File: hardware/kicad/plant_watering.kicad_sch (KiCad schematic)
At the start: 45 parts, among them J1 USB-C POWER IN (5V charger), J10 Pump2_12V, J11 Pump3_12V, J12 Pump4_12V, J13 Pump5_12V, J14 Pump6_12V, J15 Float switch (water level), J2 UI MODULE, J3 Sensor1 (GND,VCC,DIS,OUT), J4 Sensor2 (GND,VCC,DIS,OUT), J5 Sensor3 (GND,VCC,DIS,OUT), J6 Sensor4 (GND,VCC,DIS,OUT), J7 Sensor5 (GND,VCC,DIS,OUT), J8 Sensor6 (GND,VCC,DIS,OUT), J9 Pump1_12V, Q1 IRLZ44N, Q2 IRLZ44N, Q3 IRLZ44N, Q4 IRLZ44N, Q5 IRLZ44N, Q6 IRLZ44N, U1 YD-ESP32-23

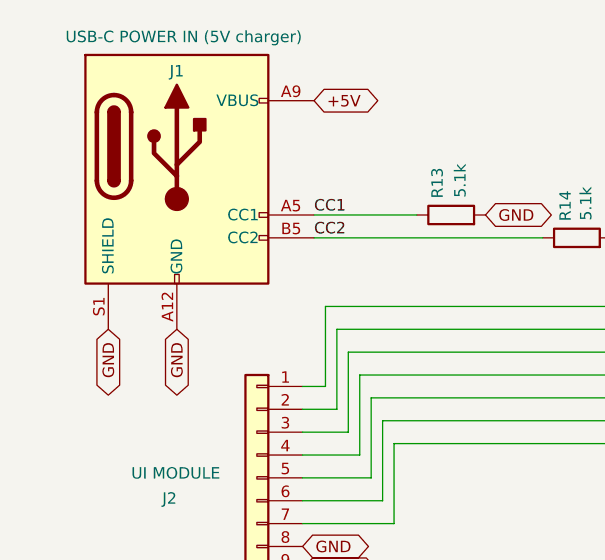
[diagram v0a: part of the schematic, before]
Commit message: Mount UI module on the PCB, panel USB-C input, extra mounting holes
- J2: replace the JST-XH 9-pin with a 1x9 2.54 mm socket plus the UI
  module's four M3 standoff holes (new UI_module_OLED_EC11 footprint);
  the module plugs in face-up left of the ESP32 and screws down
- Board widened to 143 x 112 mm for the module; UI nets rerouted,
  corner holes moved, three extra M3 holes beside J3-J8 against flex
- J1: JST-PH 6-pin for a panel-mount USB-C socket cable
- MT3608 footprint updated to measured hole spacing (26 x 13 mm)
- README/BOM: UI module photo and mounting notes, ESP pinout and
  IN-OUT jumper warning, 1:1 printable board PDF

Co-Authored-By: Claude Opus 5.5 <noreply@anthropic.com>
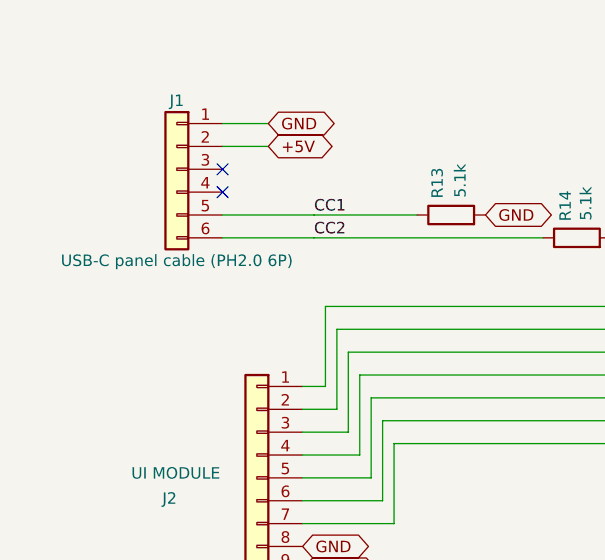
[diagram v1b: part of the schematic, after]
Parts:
- removed J1: USB-C POWER IN (5V charger), Connector_USB:USB_C_Receptacle_GCT_USB4125-xx-x-0190_6P_TopMnt_Horizontal, symbol Connector:USB_C_Receptacle_PowerOnly_6P
- added J1: USB-C panel cable (PH2.0 6P), Connector_JST:JST_PH_B6B-PH-K_1x06_P2.00mm_Vertical, symbol Connector_Generic:Conn_01x06
- J2: footprint Connector_JST:JST_XH_B9B-XH-A_1x09_P2.50mm_Vertical -> plant_watering_parts:UI_module_OLED_EC11
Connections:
- net +5V: now also J1.2 (Pin_2)
- net CC1: now also J1.5 (Pin_5)
- net CC2: now also J1.6 (Pin_6)
- net GND: now also J1.1 (Pin_1)
- no-connect marks 0 -> 2
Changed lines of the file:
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@@
 	(wire
 		(pts
+			(xy 34.29 26.67) (xy 39.37 26.67)
+		)
+		(stroke
+			(width 0)
+			(type default)
+		)
+	)
+	(wire
+		(pts
+			(xy 34.29 29.21) (xy 39.37 29.21)
+		)
+		(stroke
+			(width 0)
+			(type default)
+		)
+	)
+	(wire
+		(pts
+			(xy 34.29 36.83) (xy 44.45 36.83)
+		)
+		(stroke
+			(width 0)
+			(type default)
+		)
+	)
+	(wire
+		(pts
+			(xy 34.29 39.37) (xy 44.45 39.37)
+		)
+		(stroke
+			(width 0)
+			(type default)
+		)
+	)
+	(no_connect
+		(at 34.29 31.75)
+	)
+	(no_connect
+		(at 34.29 34.29)
+	)
+	(wire
+		(pts
 			(xy 118.11 80.01) (xy 124.46 80.01)
 		)
@@
 	(global_label "GND"
 		(shape bidirectional)
-		(at 29.21 49.53 270)
+		(at 39.37 26.67 0)
 		(effects
 			(font
 				(size 1.27 1.27)
 			)
-			(justify right)
+			(justify left)
 		)
 		(property "Intersheetrefs" "${INTERSHEET_REFS}"
-			(at 29.21 49.53 0)
+			(at 39.37 26.67 0)
 			(hide yes)
 			(show_name no)
@@
 	(global_label "+5V"
 		(shape bidirectional)
-		(at 44.45 24.13 0)
+		(at 39.37 29.21 0)
 		(effects
 			(font
@@
 		)
 		(property "Intersheetrefs" "${INTERSHEET_REFS}"
-			(at 44.45 24.13 0)
+			(at 39.37 29.21 0)
 			(hide yes)
 			(show_name no)
@@
 		)
 	)
-	(global_label "GND"
-		(shape bidirectional)
-		(at 21.59 49.53 270)
-		(effects
-			(font
-				(size 1.27 1.27)
-			)
-			(justify right)
-		)
-		(property "Intersheetrefs" "${INTERSHEET_REFS}"
-			(at 21.59 49.53 0)
-			(hide yes)
-			(show_name no)
-			(do_not_autoplace no)
-			(effects
-				(font
-					(size 1.27 1.27)
-				)
-			)
-		)
-	)
 	(global_label "+3V3"
 		(shape bidirectional)
@@
 	)
 	(symbol
-		(lib_id "Connector:USB_C_Receptacle_PowerOnly_6P")
-		(at 29.21 31.75 0)
-		(unit 1)
-		(body_style 1)
-		(exclude_from_sim no)
-		(in_bom yes)
-		(on_board yes)
-		(in_pos_files yes)
-		(dnp no)
-		(property "Reference" "J1"
-			(at 29.21 21.59 0)
-			(show_name no)
-			(do_not_autoplace no)
-			(effects
-				(font
-					(size 1.27 1.27)
-				)
-				(justify bottom)
-			)
-		)
-		(property "Value" "USB-C POWER IN (5V charger)"
-			(at 29.972 17.78 0)
-			(show_name no)
-			(do_not_autoplace no)
-			(effects
-				(font
-					(size 1.27 1.27)
-				)
-				(justify bottom)
-			)
-		)
-		(property "Footprint" "Connector_USB:USB_C_Receptacle_GCT_USB4125-xx-x-0190_6P_TopMnt_Horizontal"
-			(at 33.02 34.29 0)
-			(hide yes)
-			(show_name no)
-			(do_not_autoplace no)
-			(effects
-				(font
-					(size 1.27 1.27)
-				)
-			)
-		)
-		(property "Datasheet" "https://www.usb.org/sites/default/files/documents/usb_type-c.zip"
-			(at 29.21 31.75 0)
-			(hide yes)
-			(show_name no)
-			(do_not_autoplace no)
-			(effects
-				(font
-					(size 1.27 1.27)
-				)
-			)
-		)
-		(property "Description" "USB Power-Only 6P Type-C Receptacle connector"
-			(at 29.21 31.75 0)
-			(hide yes)
-			(show_name no)
-			(do_not_autoplace no)
-			(effects
-				(font
-					(size 1.27 1.27)
-				)
-			)
-		)
-		(pin "A12"
-		)
-		(pin "A5"
-		)
-		(pin "A9"
-		)
-		(pin "B12"
-		)
-		(pin "B5"
-		)
-		(pin "B9"
-		)
-		(pin "S1"
-		)
-		(instances
-			(project "plant_watering"
-				(path "/44c71f65-c0c8-415d-9be8-1e5a85110f51"
-					(reference "J1")
-					(unit 1)
-				)
-			)
-		)
-	)
-	(symbol
 		(lib_id "Diode:1N5819")
 		(at 254 163.83 90)
@@
 			)
 		)
-		(property "Footprint" "Connector_JST:JST_XH_B9B-XH-A_1x09_P2.50mm_Vertical"
+		(property "Footprint" "plant_watering_parts:UI_module_OLED_EC11"
 			(at 38.1 66.04 0)
 			(hide yes)
@@
           (unit 1)
         )
+      )
+    )
+  )
+    (symbol (lib_id "Connector_Generic:Conn_01x06") (at 29.21 31.75 0) (mirror y) (unit 1)
+    (body_style 1) (exclude_from_sim no) (in_bom yes) (on_board yes) (in_pos_files yes) (dnp no)
+    (property "Reference" "J1"
+      (at 29.21 24.13 0)
+      (show_name no)
+      (do_not_autoplace no)
+      (effects
+    				(font
+    					(size 1.27 1.27)
+    				)
+    			)
+    )
+    (property "Value" "USB-C panel cable (PH2.0 6P)"
+      (at 29.21 41.91 0)
+      (show_name no)
+      (do_not_autoplace no)
+      (effects
+    				(font
+    					(size 1.27 1.27)
+    				)
+    			)
+    )
+    (property "Footprint" "Connector_JST:JST_PH_B6B-PH-K_1x06_P2.00mm_Vertical"
+      (at 29.21 31.75 0)
+      (hide yes)
+      (show_name no)
+      (do_not_autoplace no)
+      (effects
+    				(font
+    					(size 1.27 1.27)
+    				)
+    			)
+    )
+    (property "Datasheet" "https://www.usb.org/sites/default/files/documents/usb_type-c.zip"
+      (at 29.21 31.75 0)
+      (hide yes)
+      (show_name no)
+      (do_not_autoplace no)
+      (effects
+    				(font
+    					(size 1.27 1.27)
+    				)
+    			)
+    )
+    (property "Description" "USB Power-Only 6P Type-C Receptacle connector"
+      (at 29.21 31.75 0)
+      (hide yes)
+      (show_name no)
+      (do_not_autoplace no)
+      (effects
+    				(font
+    					(size 1.27 1.27)
+    				)
+    			)
+    )
+    (pin "1")
+    (pin "2")
+    (pin "3")
+    (pin "4")
+    (pin "5")
+    (pin "6")
+    (instances
+      (project "plant_watering"
+        (path "/44c71f65-c0c8-415d-9be8-1e5a85110f51"
+          (reference "J1")
+          (unit 1)
+        )

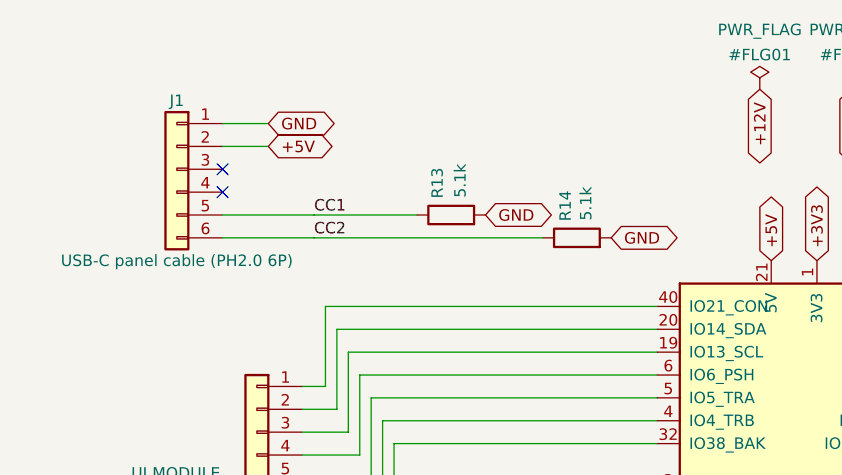
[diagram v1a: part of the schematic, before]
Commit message: Simplify USB-C power input to a 2-pin V+/V- connector
J1 becomes a JST-XH 2-pin header (1 GND, 2 +5V) for a 2-wire panel
USB-C socket. Drop the CC pull-downs R13/R14 and the CC1/CC2 nets; the
socket must provide its own 5.1k CC resistors for C-to-C chargers.
Update BOM, README and the 3D view image.

Co-Authored-By: Claude Opus 5.5 <noreply@anthropic.com>
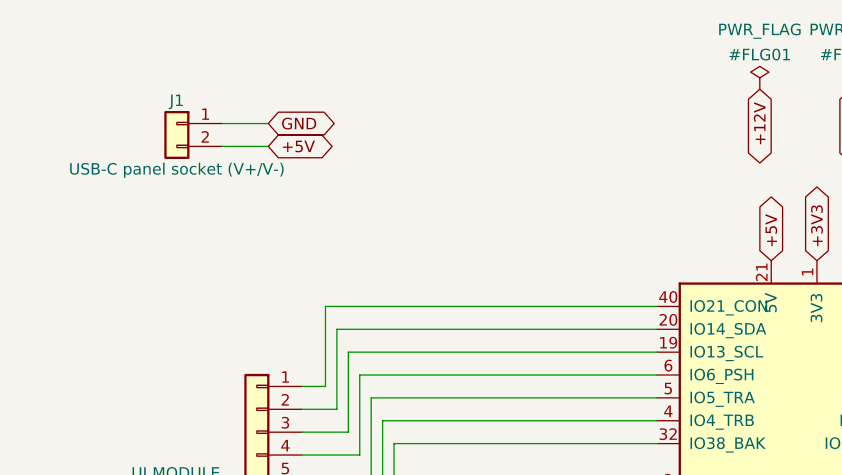
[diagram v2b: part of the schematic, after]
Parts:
- removed R13, R14: 5.1k, Resistor_THT:R_Axial_DIN0207_L6.3mm_D2.5mm_P10.16mm_Horizontal, symbol Device:R
- J1: value USB-C panel cable (PH2.0 6P) -> USB-C panel socket (V+/V-); footprint Connector_JST:JST_PH_B6B-PH-K_1x06_P2.00mm_Vertical -> Connector_JST:JST_XH_B2B-XH-A_1x02_P2.50mm_Vertical; symbol Connector_Generic:Conn_01x06 -> Connector_Generic:Conn_01x02
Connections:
- removed net CC1: J1.5 (Pin_5)
- removed net CC2: J1.6 (Pin_6)
- no-connect marks 2 -> 0
